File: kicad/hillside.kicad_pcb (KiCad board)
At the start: 2 copper layers, 136.6 x 97.9 mm, 65 parts, among them J1 Haptic, J2 TRRS, J3 Bat_Pos, J4 Bat_GND, K1 SW_Key, K10 SW_Key, K11 SW_Key, K12 SW_Key, K13 SW_Key, K14 SW_Key, K15 SW_Key, K16 SW_Key, K17 SW_Key, K18 SW_Key, K19 SW_Key, K2 SW_Key, K20 SW_Rotary, K21 SW_Key, K22 SW_Key, K23 SW_Key, K24 SW_Key, K3 SW_Key, K4 SW_Key, K5 SW_Key, K6 SW_Key, K7 SW_Key, K8 SW_Key, K9 SW_Key, SW1 Reset, SW2 SW_Power, U1 ProMicro_r

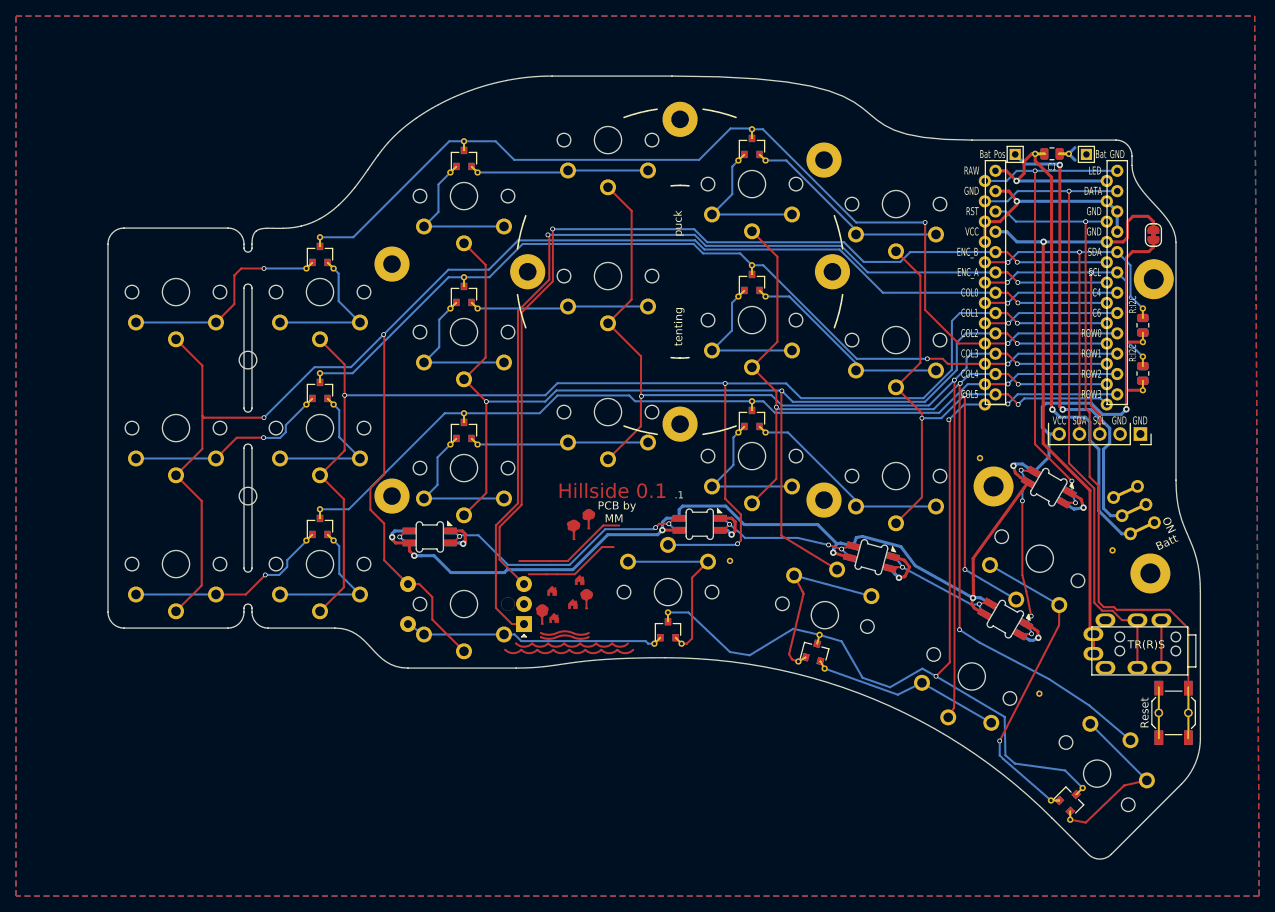
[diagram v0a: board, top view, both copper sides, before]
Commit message: Board edgecut 0.25 mm out to match keycap outline
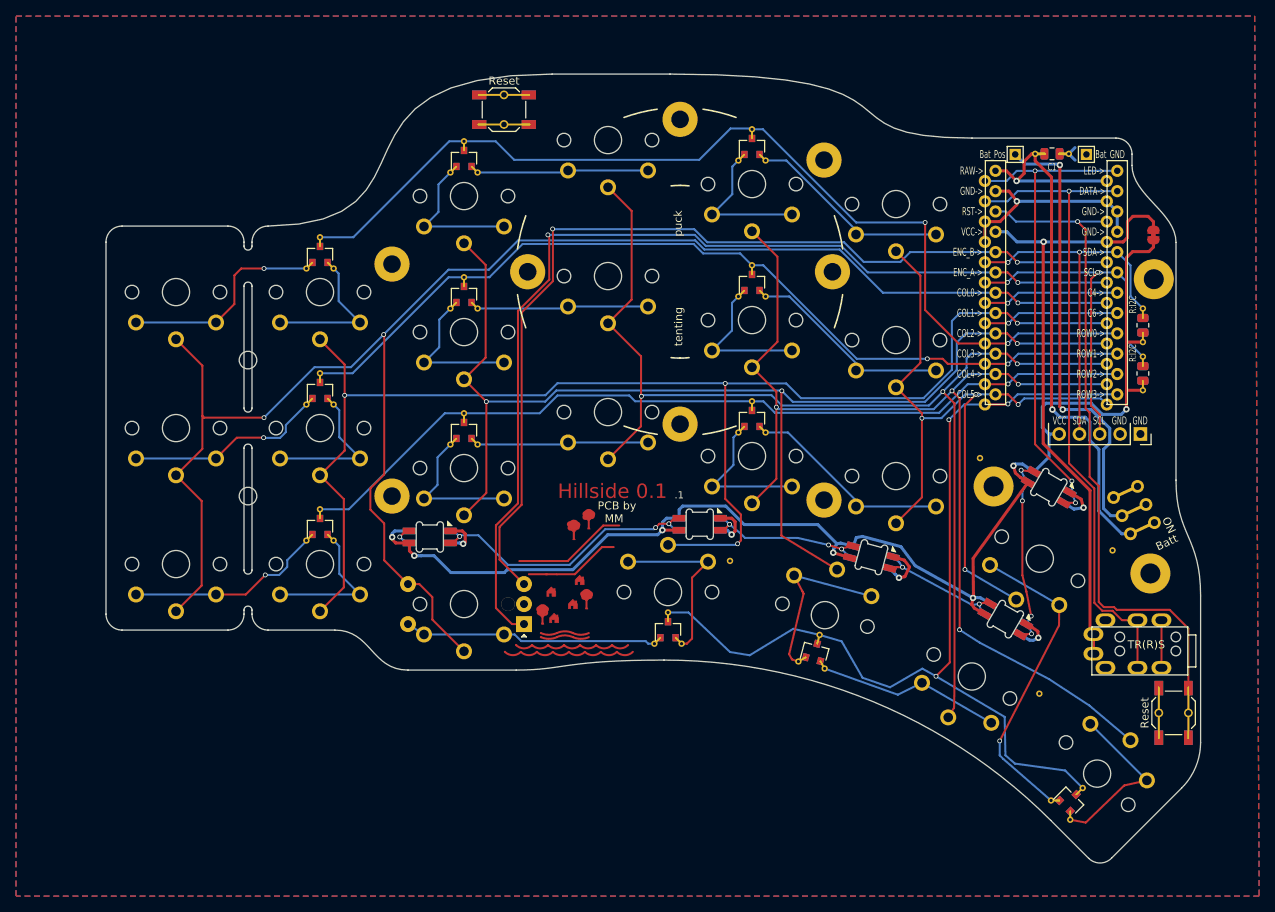
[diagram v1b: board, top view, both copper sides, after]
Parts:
- added SW1: Reset, hillside_basic:SW_SPST_SKQG_WithStem, F.Cu at (137.0, 59.2)
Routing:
- net col3: track 145.0 -> 144.1 mm
- net col5: track 94.0 -> 94.6 mm
- net col4: track 139.3 -> 138.7 mm
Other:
- board size 136.6 x 97.9 mm -> 136.8 x 98.6 mm

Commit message: Improve paths to ground
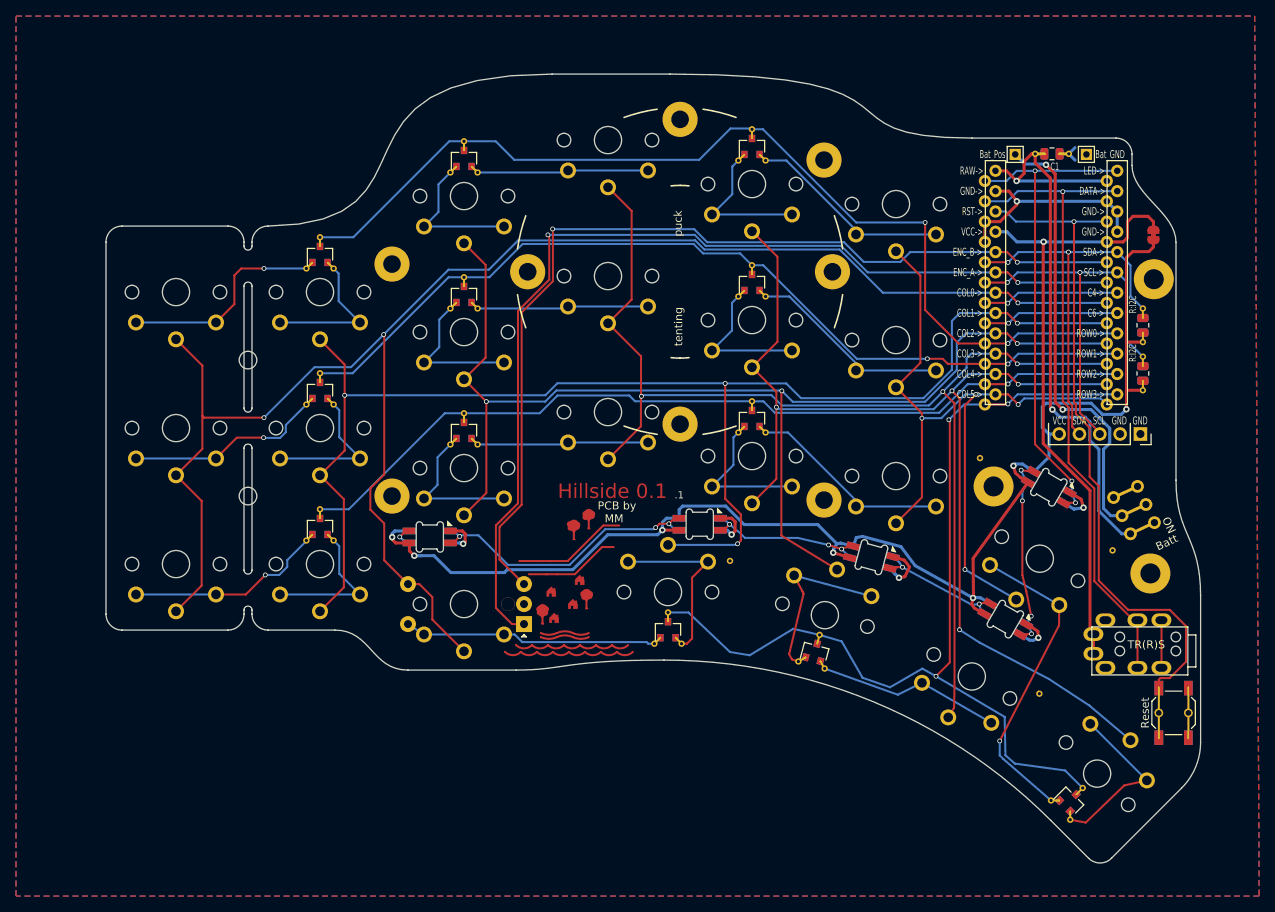
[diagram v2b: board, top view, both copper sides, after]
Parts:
- removed the SW1 at (137.0, 59.2)
- turned SW1 to 90 degrees
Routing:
- net data: track 82.1 -> 80.8 mm
- net bat+: track 56.7 -> 55.7 mm
- net SDA: track 48.2 -> 48.8 mm
- net reset: track 83.1 -> 83.7 mm

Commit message: Two battery pad options. PCB to MCU alignment note
- Clearer track routing, Parallel tracks split into groups by function,
  not all clumped.
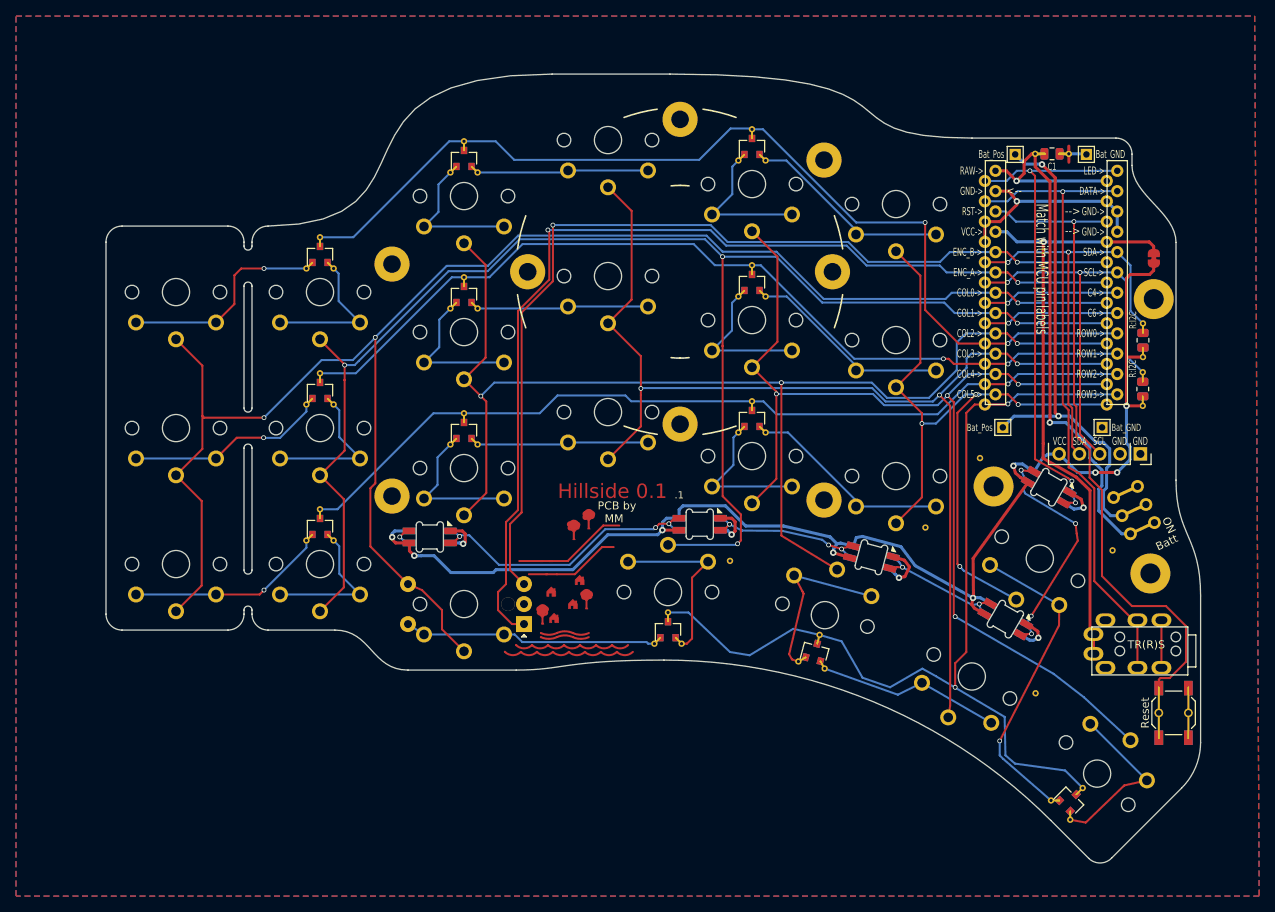
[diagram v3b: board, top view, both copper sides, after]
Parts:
- removed the H6 at (105.0, 90.5)
- removed the H7 at (105.0, 107.5)
- added J5: Bat_Pos, hillside_basic:1pin_conn, F.Cu at (199.3, 98.9)
- added J6: Bat_GND, hillside_basic:1pin_conn, F.Cu at (211.8, 98.9)
- added V1: Via, hillside_basic:VIA-0.8mm, F.Cu at (189.7, 111.4)
- moved JP1 2.91 mm to (218.2, 77.8)
- moved J1 2.49 mm to (211.5, 91.1)
- moved R1 1.95 mm to (216.8, 94.1)
- moved R2 1.87 mm to (216.9, 88.0)
- moved V4 0.47 mm to (203.4, 132.2)
- renumbered H8 to H6, H9 to H7
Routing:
- net col1: track 173.9 -> 190.8 mm
- net bat+: track 55.7 -> 62.3 mm
- net Net-(D1-Pad2): track 24.7 -> 29.8 mm
- net SCL: track 50.2 -> 54.6 mm
- net SDA: track 48.8 -> 53.1 mm
- net VCC_ACC: track 170.5 -> 166.4 mm, vias 7 -> 9
- net GND: track 56.5 -> 58.5 mm
- net VCC: track 78.2 -> 76.2 mm
- net col2: track 149.6 -> 151.4 mm
- net LED: track 61.4 -> 62.4 mm
- net col3: track 144.1 -> 143.4 mm
- net enc_a: track 126.1 -> 126.8 mm
- net reset: track 83.7 -> 83.1 mm
- net col5: track 94.6 -> 95.2 mm
- net col4: track 138.7 -> 138.2 mm
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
